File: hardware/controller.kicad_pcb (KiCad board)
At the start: 2 copper layers, 73.7 x 76.2 mm, 65 parts, among them J1 USB_B_Micro, J2 AVR-ISP-6, Q1 AO3402, Q10 AO3402, Q11 AO3402, Q12 AO3402, Q13 AO3402, Q14 AO3402, Q15 AO3402, Q16 AO3402, Q2 AO3402, Q3 AO3402, Q4 AO3402, Q5 AO3402, Q6 AO3402, Q7 AO3402, Q8 AO3402, Q9 AO3402, SW1 SW_Push_NO_NC_LED, SW10 SW_Push_NO_NC_LED, SW11 SW_Push_NO_NC_LED, SW12 SW_Push_NO_NC_LED, SW13 SW_Push_NO_NC_LED, SW14 SW_Push_NO_NC_LED, SW15 SW_Push_NO_NC_LED, SW16 SW_Push_NO_NC_LED, SW2 SW_Push_NO_NC_LED, SW3 SW_Push_NO_NC_LED, SW4 SW_Push_NO_NC_LED, SW5 SW_Push_NO_NC_LED, SW6 SW_Push_NO_NC_LED, SW7 SW_Push_NO_NC_LED, SW8 SW_Push_NO_NC_LED, SW9 SW_Push_NO_NC_LED, U1 CH340C, U2 ATmega328-AU, U3 MCP23017_SS, U4 PCA9685PW, Y1 14.7456 Mhz

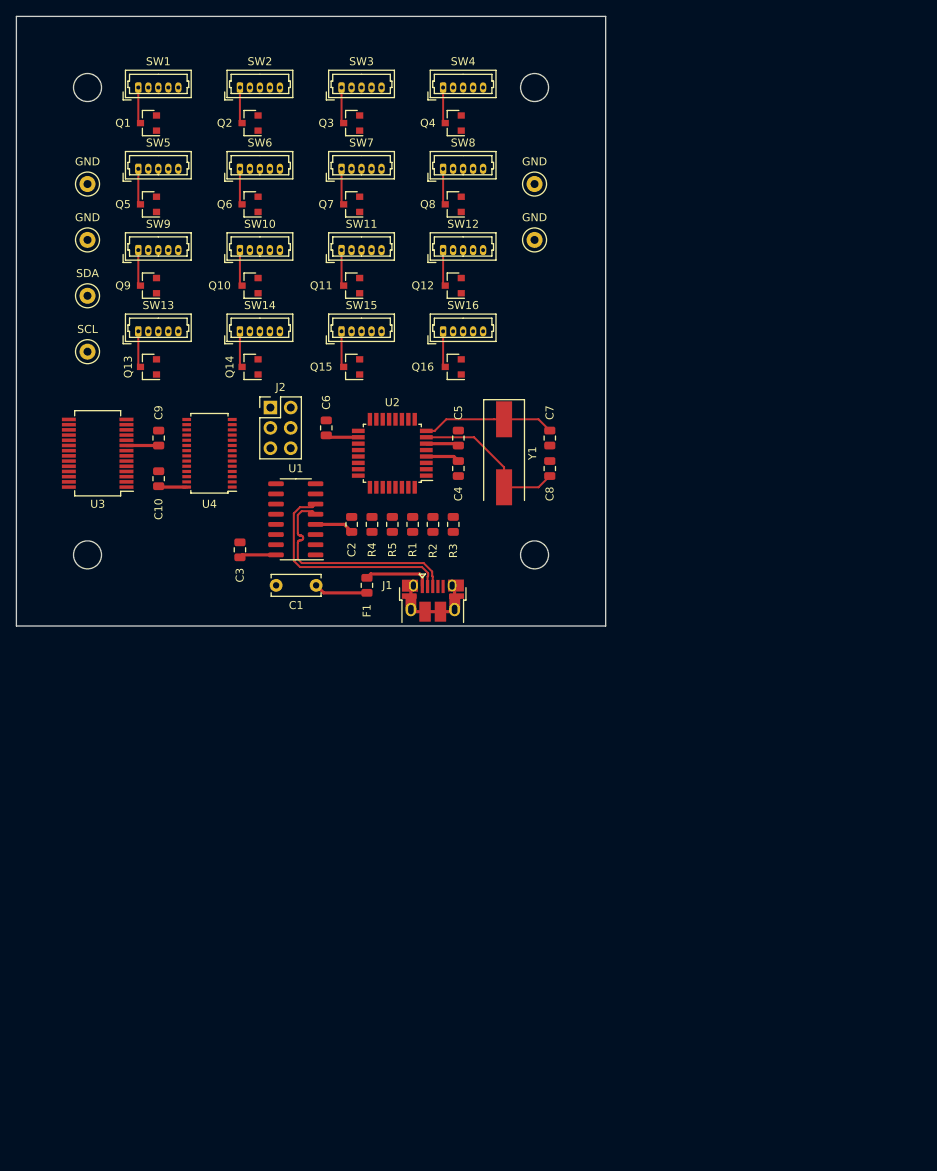
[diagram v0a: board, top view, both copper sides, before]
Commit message: create routing-friendly PCB layout and route it manually
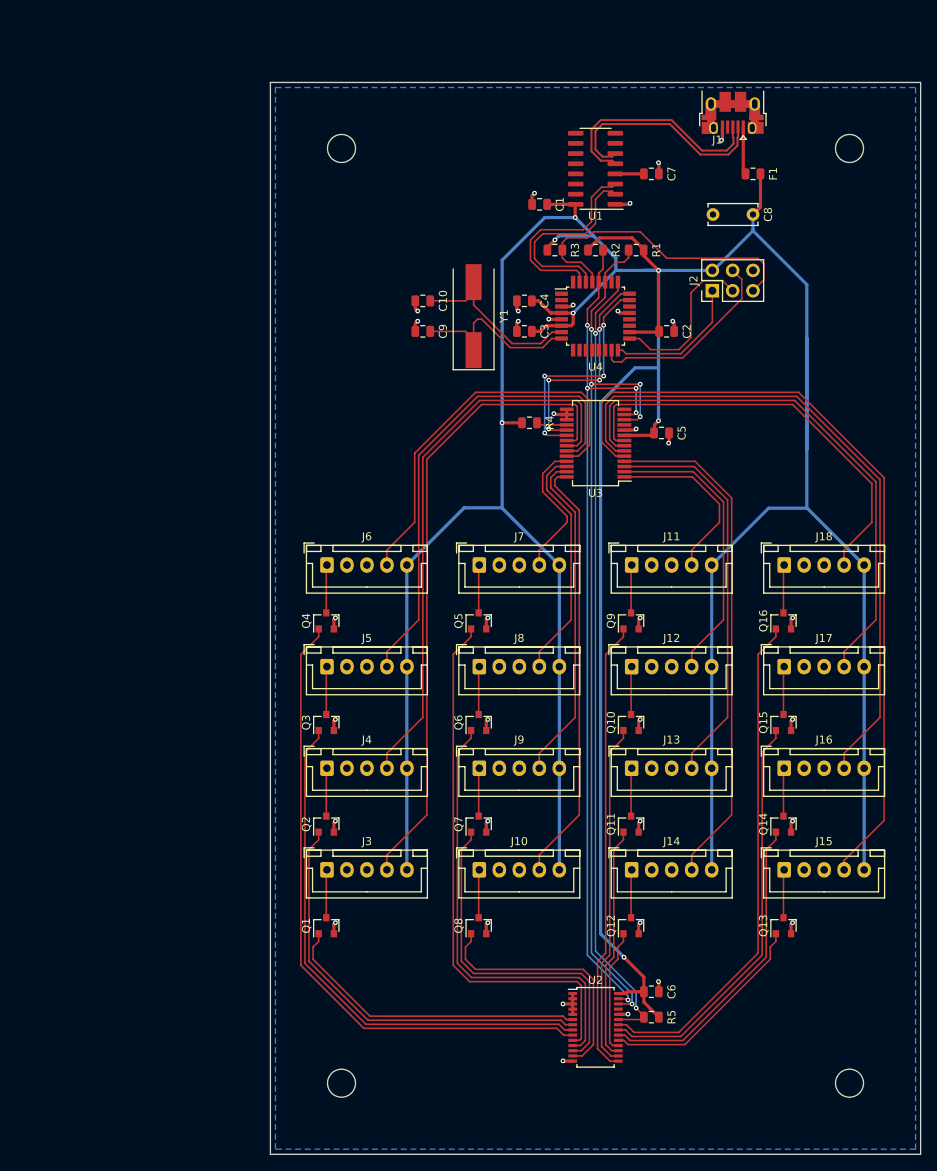
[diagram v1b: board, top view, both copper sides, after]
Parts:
- removed SW1, SW10, SW11, SW12, SW13, SW14, SW15, SW16, SW2, SW3, SW4, SW5, SW6, SW7, SW8, SW9: SW_Push_NO_NC_LED, Connector_Molex:Molex_PicoBlade_53047-0510_1x05_P1.25mm_Vertical
- removed TP1: SDA, TestPoint:TestPoint_Loop_D1.80mm_Drill1.0mm_Beaded
- removed TP2: SCL, TestPoint:TestPoint_Loop_D1.80mm_Drill1.0mm_Beaded
- removed TP3, TP4, TP5, TP6: GND, TestPoint:TestPoint_Loop_D1.80mm_Drill1.0mm_Beaded
- added J10: Conn_01x05_Male, Connector_JST:JST_XH_B5B-XH-A_1x05_P2.50mm_Vertical, F.Cu at (115.0, 147.3)
- added J11: Conn_01x05_Male, Connector_JST:JST_XH_B5B-XH-A_1x05_P2.50mm_Vertical, F.Cu at (134.1, 109.2)
- added J12: Conn_01x05_Male, Connector_JST:JST_XH_B5B-XH-A_1x05_P2.50mm_Vertical, F.Cu at (134.1, 121.9)
- added J13: Conn_01x05_Male, Connector_JST:JST_XH_B5B-XH-A_1x05_P2.50mm_Vertical, F.Cu at (134.1, 134.6)
- added J14: Conn_01x05_Male, Connector_JST:JST_XH_B5B-XH-A_1x05_P2.50mm_Vertical, F.Cu at (134.1, 147.3)
- added J15: Conn_01x05_Male, Connector_JST:JST_XH_B5B-XH-A_1x05_P2.50mm_Vertical, F.Cu at (153.1, 147.3)
- added J16: Conn_01x05_Male, Connector_JST:JST_XH_B5B-XH-A_1x05_P2.50mm_Vertical, F.Cu at (153.1, 134.6)
- added J17: Conn_01x05_Male, Connector_JST:JST_XH_B5B-XH-A_1x05_P2.50mm_Vertical, F.Cu at (153.1, 121.9)
- added J18: Conn_01x05_Male, Connector_JST:JST_XH_B5B-XH-A_1x05_P2.50mm_Vertical, F.Cu at (153.1, 109.2)
- added J3: Conn_01x05_Male, Connector_JST:JST_XH_B5B-XH-A_1x05_P2.50mm_Vertical, F.Cu at (96.0, 147.3)
- added J4: Conn_01x05_Male, Connector_JST:JST_XH_B5B-XH-A_1x05_P2.50mm_Vertical, F.Cu at (96.0, 134.6)
- added J5: Conn_01x05_Male, Connector_JST:JST_XH_B5B-XH-A_1x05_P2.50mm_Vertical, F.Cu at (96.0, 121.9)
- added J6: Conn_01x05_Male, Connector_JST:JST_XH_B5B-XH-A_1x05_P2.50mm_Vertical, F.Cu at (96.0, 109.2)
- added J7: Conn_01x05_Male, Connector_JST:JST_XH_B5B-XH-A_1x05_P2.50mm_Vertical, F.Cu at (115.0, 109.2)
- added J8: Conn_01x05_Male, Connector_JST:JST_XH_B5B-XH-A_1x05_P2.50mm_Vertical, F.Cu at (115.0, 121.9)
- added J9: Conn_01x05_Male, Connector_JST:JST_XH_B5B-XH-A_1x05_P2.50mm_Vertical, F.Cu at (115.0, 134.6)
- C1: value 10u -> 100n; footprint Capacitor_THT:C_Disc_D6.0mm_W2.5mm_P5.00mm -> Capacitor_SMD:C_0805_2012Metric
- C10, C9: value 100n -> 22p
- C7: value 22p -> 100n
- C8: value 22p -> 10u; footprint Capacitor_SMD:C_0805_2012Metric -> Capacitor_THT:C_Disc_D6.0mm_W2.5mm_P5.00mm
- U2: value ATmega328-AU -> PCA9685PW; footprint Package_QFP:TQFP-32_7x7mm_P0.8mm -> Package_SO:TSSOP-28_4.4x9.7mm_P0.65mm
- U4: value PCA9685PW -> ATmega328-AU; footprint Package_SO:TSSOP-28_4.4x9.7mm_P0.65mm -> Package_QFP:TQFP-32_7x7mm_P0.8mm
- moved Q13 105.7 mm to (153.0, 154.3), turned to 90 degrees
- moved Q1 102.8 mm to (95.9, 154.3), turned to 90 degrees
- moved Q8 90.2 mm to (114.9, 154.3), turned to 90 degrees
- moved Q2 88.1 mm to (95.9, 141.6), turned to 90 degrees
- moved Q14 87.8 mm to (153.0, 141.6), turned to 90 degrees
- moved Q12 83.0 mm to (134.0, 154.3), turned to 90 degrees
- moved C6 81.4 mm to (136.5, 162.6), turned to 0 degrees
- moved Q7 79.1 mm to (114.9, 141.6), turned to 90 degrees
- moved H4 76.9 mm to (161.3, 174.0)
- moved U2 76.1 mm to (129.5, 167.0), turned to 0 degrees
- moved Q11 75.8 mm to (134.0, 141.6), turned to 90 degrees
- moved Q3 75.0 mm to (95.9, 128.9), turned to 90 degrees
- moved Q9 73.5 mm to (134.0, 116.2), turned to 90 degrees
- moved H3 73.3 mm to (97.8, 174.0)
- moved Q10 72.5 mm to (134.0, 128.9), turned to 90 degrees
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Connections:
- C10 pad 1: +5V -> XTAL1
- C2 pad 1: GND -> +5V
- C2 pad 2: Net-(C2-Pad2) -> GND
- C7 pad 1: XTAL2 -> GND
- C7 pad 2: GND -> Net-(C7-Pad2)
- C8 pad 1: XTAL1 -> +5V
- C9 pad 1: +5V -> XTAL2
- Q10 pad 1: LEDx6 -> LEDx9
- Q12 pad 1: LEDxE -> LEDxB
- Q13 pad 1: LEDx3 -> LEDxC
- Q14 pad 1: LEDx7 -> LEDxD
- Q15 pad 1: LEDxB -> LEDxE
- Q2 pad 1: LEDx4 -> LEDx1
- Q3 pad 1: LEDx8 -> LEDx2
- Q4 pad 1: LEDxC -> LEDx3
- Q5 pad 1: LEDx1 -> LEDx4
- Q7 pad 1: LEDx9 -> LEDx6
- Q8 pad 1: LEDxD -> LEDx7
- Q9 pad 1: LEDx2 -> LEDx8
- R4 pad 1: GND -> +5V
- U1 pad 4: Net-(C2-Pad2) -> Net-(C7-Pad2)
- U2 pad 1: (no net) -> GND
- U2 pad 10: (no net) -> LEDx4
- U2 pad 11: (no net) -> LEDx5
- U2 pad 12: (no net) -> LEDx6
- U2 pad 13: (no net) -> LEDx7
- U2 pad 14: (no net) -> GND
- U2 pad 15: MOSI -> LEDx8
- U2 pad 16: MISO -> LEDx9
- U2 pad 17: SCK -> LEDxA
- U2 pad 18: +5V -> LEDxB
- U2 pad 19: (no net) -> LEDxC
- U2 pad 2: (no net) -> GND
- U2 pad 20: (no net) -> LEDxD
- U2 pad 21: GND -> LEDxE
- U2 pad 22: (no net) -> LEDxF
- U2 pad 23: INTA -> PCA9685.~OE
- U2 pad 24: INTB -> GND
- U2 pad 25: MCP23017.~RESET -> (no net)
- U2 pad 26: PCA9685.~OE -> SCL
- U2 pad 27: SCL -> SDA
- U2 pad 28: SDA -> +5V
- U2 pad 4: +5V -> GND
- U2 pad 6: +5V -> LEDx0
- U2 pad 7: XTAL1 -> LEDx1
- U2 pad 8: XTAL2 -> LEDx2
- U2 pad 9: (no net) -> LEDx3
- U4 pad 1: GND -> (no net)
- U4 pad 10: LEDx4 -> (no net)
- U4 pad 11: LEDx5 -> (no net)
- U4 pad 12: LEDx6 -> (no net)
- U4 pad 13: LEDx7 -> (no net)
- U4 pad 14: GND -> (no net)
- U4 pad 15: LEDx8 -> MOSI
- U4 pad 16: LEDx9 -> MISO
- U4 pad 17: LEDxA -> SCK
- U4 pad 18: LEDxB -> +5V
- U4 pad 19: LEDxC -> (no net)
- U4 pad 2: GND -> (no net)
- U4 pad 20: LEDxD -> (no net)
- U4 pad 21: LEDxE -> GND
- U4 pad 22: LEDxF -> (no net)
- U4 pad 23: PCA9685.~OE -> INTA
- U4 pad 24: GND -> INTB
- U4 pad 25: (no net) -> PCA9685.~OE
- U4 pad 26: SCL -> (no net)
- U4 pad 27: SDA -> SCL
- U4 pad 28: +5V -> SDA
- U4 pad 4: GND -> +5V
- U4 pad 6: LEDx0 -> +5V
- U4 pad 7: LEDx1 -> XTAL1
- U4 pad 8: LEDx2 -> XTAL2
- U4 pad 9: LEDx3 -> (no net)
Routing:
- net +5V: track 31.4 -> 507.8 mm, vias 0 -> 7
- net SCL: track 0.00 -> 112.9 mm, vias 0 -> 5
- net SDA: track 0.00 -> 108.6 mm, vias 0 -> 5
- net BTNxC: track 0.00 -> 99.9 mm
- net PCA9685.~OE: track 0.00 -> 98.9 mm, vias 0 -> 2
- net BTNxD: track 0.00 -> 84.3 mm
- net BTNx0: track 0.00 -> 80.6 mm
- net LEDx3: track 0.00 -> 80.6 mm
- net BTNx1: track 0.00 -> 70.3 mm
- net BTNxE: track 0.00 -> 68.9 mm
- net LEDx4: track 0.00 -> 67.8 mm
- net LEDx2: track 0.00 -> 66.7 mm
- net BTNxB: track 0.00 -> 63.9 mm
- net LEDxF: track 0.00 -> 63.4 mm
- net BTNx2: track 0.00 -> 60.1 mm
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- added copper zone on B.Cu, net GND
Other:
- board size 73.7 x 76.2 mm -> 81.3 x 134 mm
- net class Default: clearance 0.15 -> 0.1; trace_width 0.25 -> 0.2
- net class Shield added: clearance 0.2, trace_width 1, via_dia 0.6, via_drill 0.3
- rule trace_clearance: 0.15 -> 0.1

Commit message: change USB connector, finalize PCB shape
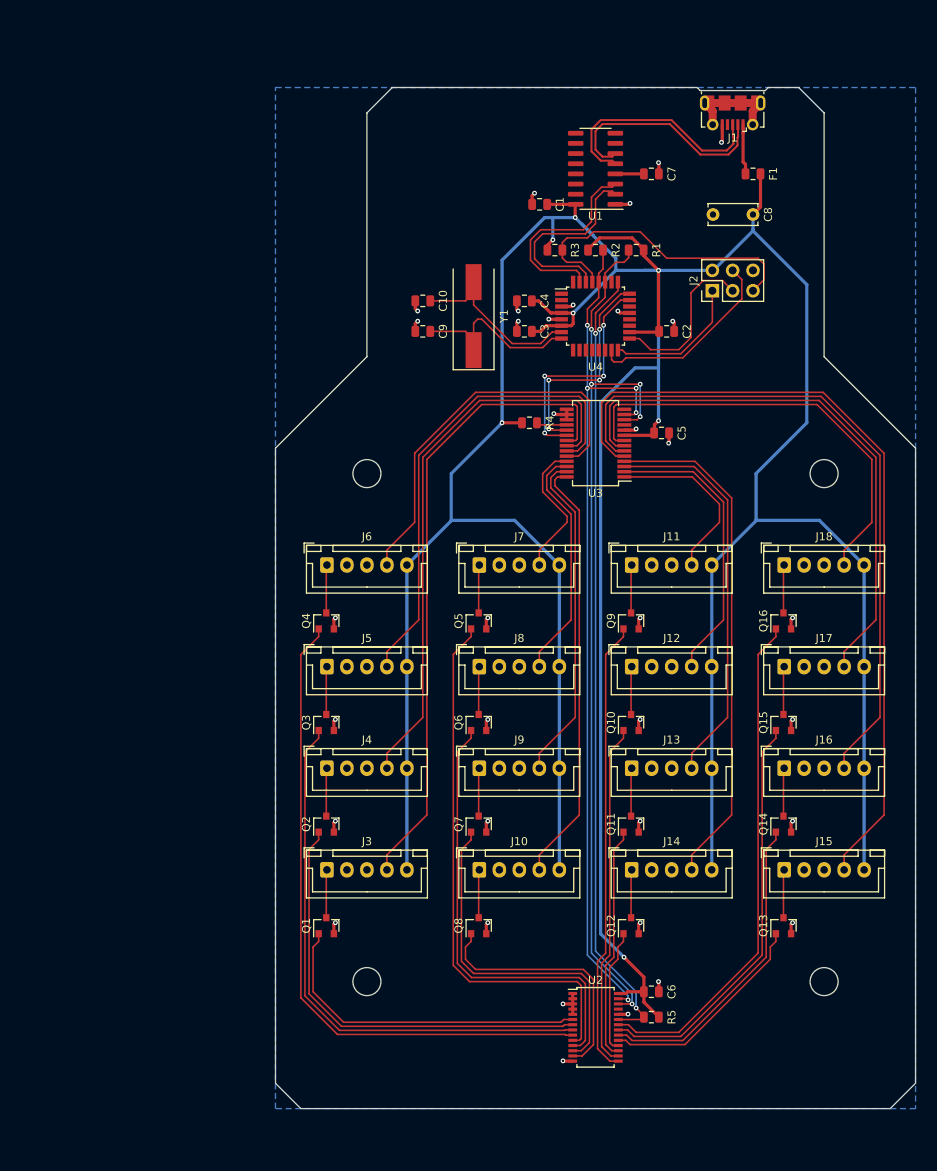
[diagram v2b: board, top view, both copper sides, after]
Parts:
- J1: footprint Connector_USB:USB_Micro-B_Amphenol_10103594-0001LF_Horizontal -> Connector_USB:USB_Micro-B_Molex-105017-0001
- moved H1 40.8 mm to (101.0, 97.8)
- moved H2 40.8 mm to (158.1, 97.8)
- moved H3 13.1 mm to (101.0, 161.3)
- moved H4 13.1 mm to (158.1, 161.3)
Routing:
- net +5V: track 507.8 -> 499.4 mm
- net LEDx0: track 39.1 -> 41.7 mm
- net LEDx1: track 52.9 -> 55.4 mm
- net LEDx2: track 66.7 -> 69.2 mm
- net LEDx3: track 80.6 -> 82.9 mm
- net BTNxD: track 84.3 -> 86.1 mm
- net BTNxF: track 53.4 -> 55.2 mm
- net BTNxC: track 99.9 -> 101.6 mm
- net BTNxE: track 68.9 -> 70.7 mm
- net Net-(J1-Pad6): track 11.7 -> 12.6 mm
- net GND: track 54.8 -> 55.3 mm
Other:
- board size 81.3 x 134 mm -> 80 x 127.6 mm

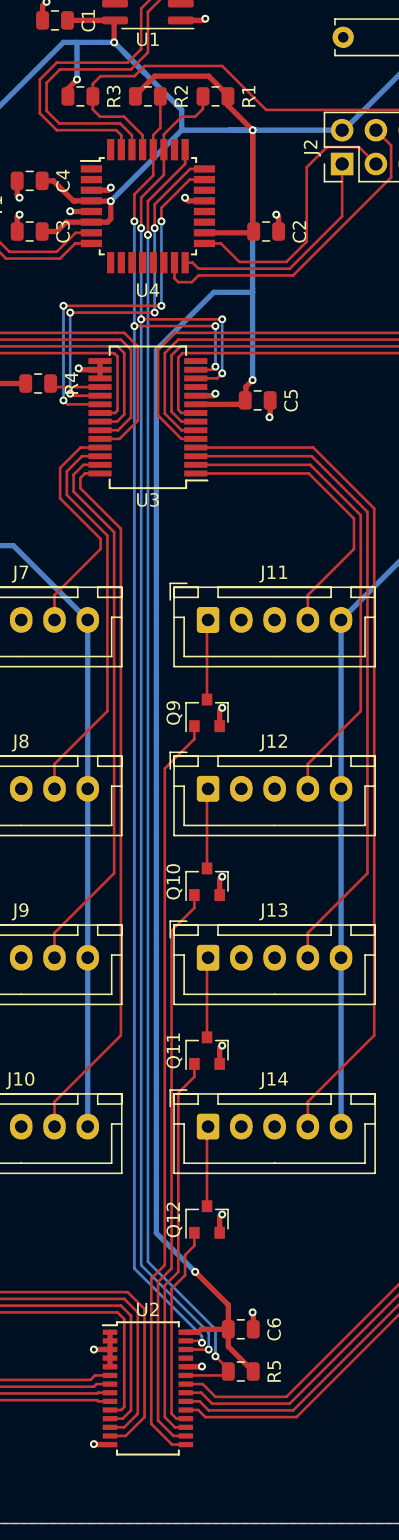
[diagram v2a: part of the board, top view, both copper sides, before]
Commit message: fix assignment of SCL and SDA pins on ATmega328p
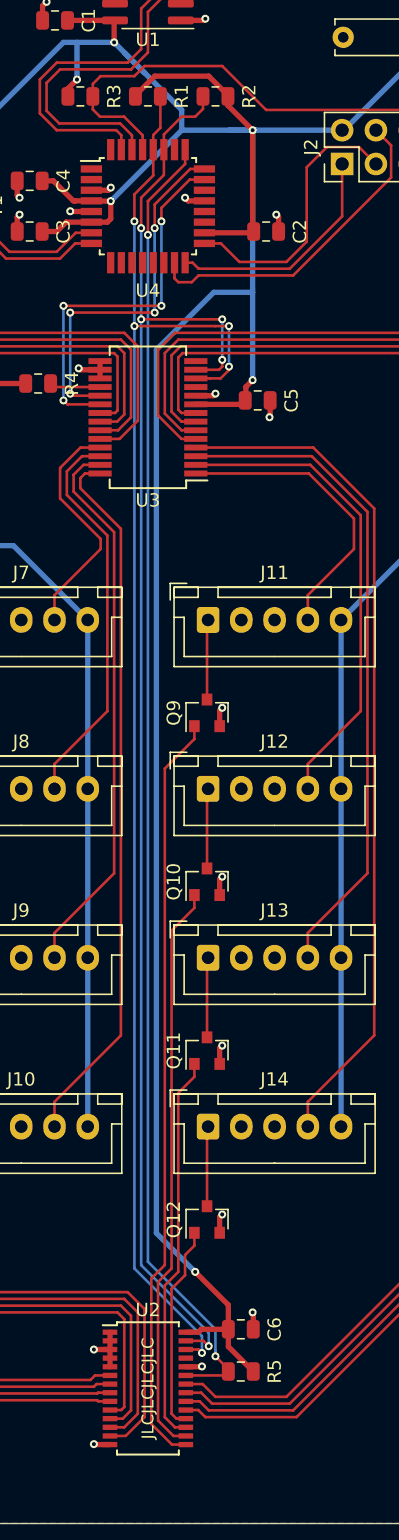
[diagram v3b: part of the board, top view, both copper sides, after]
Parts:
- U4: value ATmega328-AU -> ATmega328P-MU
- moved R1 5.08 mm to (129.5, 69.8), turned to 180 degrees
- moved R2 5.08 mm to (134.6, 69.8), turned to 0 degrees
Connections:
- U4 pad 27: SCL -> SDA
- U4 pad 28: SDA -> SCL
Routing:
- net SDA: track 108.6 -> 112.2 mm
- net SCL: track 112.9 -> 111.9 mm
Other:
- board text added: "JLCJLCJLCJLC"

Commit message: use 36pF capacitors for crystal
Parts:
- C10, C9: value 22p -> 36p
- U4: value ATmega328P-MU -> ATmega328P-AU
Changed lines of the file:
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@@
     (add_net MISO)
     (add_net MOSI)
+    (add_net "Net-(J1-Pad4)")
     (add_net "Net-(J10-Pad1)")
+    (add_net "Net-(J10-Pad2)")
     (add_net "Net-(J11-Pad1)")
+    (add_net "Net-(J11-Pad2)")
     (add_net "Net-(J12-Pad1)")
+    (add_net "Net-(J12-Pad2)")
     (add_net "Net-(J13-Pad1)")
+    (add_net "Net-(J13-Pad2)")
     (add_net "Net-(J14-Pad1)")
+    (add_net "Net-(J14-Pad2)")
     (add_net "Net-(J15-Pad1)")
+    (add_net "Net-(J15-Pad2)")
     (add_net "Net-(J16-Pad1)")
+    (add_net "Net-(J16-Pad2)")
     (add_net "Net-(J17-Pad1)")
+    (add_net "Net-(J17-Pad2)")
     (add_net "Net-(J18-Pad1)")
+    (add_net "Net-(J18-Pad2)")
     (add_net "Net-(J3-Pad1)")
+    (add_net "Net-(J3-Pad2)")
     (add_net "Net-(J4-Pad1)")
+    (add_net "Net-(J4-Pad2)")
     (add_net "Net-(J5-Pad1)")
+    (add_net "Net-(J5-Pad2)")
     (add_net "Net-(J6-Pad1)")
+    (add_net "Net-(J6-Pad2)")
     (add_net "Net-(J7-Pad1)")
+    (add_net "Net-(J7-Pad2)")
     (add_net "Net-(J8-Pad1)")
+    (add_net "Net-(J8-Pad2)")
     (add_net "Net-(J9-Pad1)")
+    (add_net "Net-(J9-Pad2)")
+    (add_net "Net-(U1-Pad10)")
+    (add_net "Net-(U1-Pad11)")
+    (add_net "Net-(U1-Pad12)")
+    (add_net "Net-(U1-Pad13)")
+    (add_net "Net-(U1-Pad14)")
+    (add_net "Net-(U1-Pad15)")
+    (add_net "Net-(U1-Pad7)")
+    (add_net "Net-(U1-Pad8)")
+    (add_net "Net-(U1-Pad9)")
+    (add_net "Net-(U2-Pad25)")
+    (add_net "Net-(U3-Pad11)")
+    (add_net "Net-(U3-Pad14)")
+    (add_net "Net-(U4-Pad1)")
+    (add_net "Net-(U4-Pad10)")
+    (add_net "Net-(U4-Pad11)")
+    (add_net "Net-(U4-Pad12)")
+    (add_net "Net-(U4-Pad13)")
+    (add_net "Net-(U4-Pad14)")
+    (add_net "Net-(U4-Pad19)")
+    (add_net "Net-(U4-Pad2)")
+    (add_net "Net-(U4-Pad20)")
+    (add_net "Net-(U4-Pad22)")
+    (add_net "Net-(U4-Pad26)")
+    (add_net "Net-(U4-Pad32)")
+    (add_net "Net-(U4-Pad9)")
     (add_net PCA9685.~OE)
     (add_net RXD)
@@
       (effects (font (size 1 1) (thickness 0.15)))
     )
-    (fp_text value ATmega328P-MU (at 0 6.05) (layer F.Fab)
+    (fp_text value ATmega328P-AU (at 0 6.05) (layer F.Fab)
       (effects (font (size 1 1) (thickness 0.15)))
     )
@@
       (effects (font (size 1 1) (thickness 0.15)))
     )
-    (fp_text value 22p (at 0 1.65) (layer F.Fab)
+    (fp_text value 36p (at 0 1.65) (layer F.Fab)
       (effects (font (size 1 1) (thickness 0.15)))
     )
@@
       (effects (font (size 1 1) (thickness 0.15)))
     )
-    (fp_text value 22p (at 0 1.65) (layer F.Fab)
+    (fp_text value 36p (at 0 1.65) (layer F.Fab)
       (effects (font (size 1 1) (thickness 0.15)))
     )
@@
   (segment (start 129.536 54.967554) (end 129.536 57.300446) (width 0.25) (layer F.Cu) (net 11))
   (segment (start 147.285 55.782501) (end 147.285 56.776554) (width 0.25) (layer F.Cu) (net 11))
-  (segment (start 133.6825 70.7875) (end 133.6825 69.85) (width 0.2) (layer F.Cu) (net 13))
-  (segment (start 133.096 71.374) (end 133.6825 70.7875) (width 0.2) (layer F.Cu) (net 13))
-  (segment (start 132.08 71.374) (end 133.096 71.374) (width 0.2) (layer F.Cu) (net 13))
-  (segment (start 130.74 72.714) (end 132.08 71.374) (width 0.2) (layer F.Cu) (net 13))
-  (segment (start 130.74 73.855) (end 130.74 72.714) (width 0.2) (layer F.Cu) (net 13))
-  (via (at 129.032 79.756) (size 0.6) (drill 0.3) (layers F.Cu B.Cu) (net 13))
-  (segment (start 130.74 75.762) (end 130.74 73.855) (width 0.2) (layer F.Cu) (net 13))
-  (segment (start 129.032 77.47) (end 130.74 75.762) (width 0.2) (layer F.Cu) (net 13))
-  (segment (start 129.032 79.756) (end 129.032 77.47) (width 0.2) (layer F.Cu) (net 13))
-  (segment (start 129.032 79.756) (end 129.032 86.614) (width 0.2) (layer B.Cu) (net 13))
-  (segment (start 129.032 157.734) (end 134.112 162.814) (width 0.2) (layer B.Cu) (net 13))
-  (segment (start 129.032 86.614) (end 129.032 157.734) (width 0.2) (layer B.Cu) (net 13))
   (segment (start 130.4775 72.2145) (end 130.4775 69.85) (width 0.2) (layer F.Cu) (net 12))
   (segment (start 129.94 72.752) (end 130.4775 72.2145) (width 0.2) (layer F.Cu) (net 12))
@@
   (segment (start 135.636 90.424) (end 135.005 91.055) (width 0.2) (layer F.Cu) (net 12))
   (segment (start 135.636 90.17) (end 135.636 90.424) (width 0.2) (layer F.Cu) (net 12))
+  (segment (start 133.6825 70.7875) (end 133.6825 69.85) (width 0.2) (layer F.Cu) (net 13))
+  (segment (start 133.096 71.374) (end 133.6825 70.7875) (width 0.2) (layer F.Cu) (net 13))
+  (segment (start 132.08 71.374) (end 133.096 71.374) (width 0.2) (layer F.Cu) (net 13))
+  (segment (start 130.74 72.714) (end 132.08 71.374) (width 0.2) (layer F.Cu) (net 13))
+  (segment (start 130.74 73.855) (end 130.74 72.714) (width 0.2) (layer F.Cu) (net 13))
+  (via (at 129.032 79.756) (size 0.6) (drill 0.3) (layers F.Cu B.Cu) (net 13))
+  (segment (start 130.74 75.762) (end 130.74 73.855) (width 0.2) (layer F.Cu) (net 13))
+  (segment (start 129.032 77.47) (end 130.74 75.762) (width 0.2) (layer F.Cu) (net 13))
+  (segment (start 129.032 79.756) (end 129.032 77.47) (width 0.2) (layer F.Cu) (net 13))
+  (segment (start 129.032 79.756) (end 129.032 86.614) (width 0.2) (layer B.Cu) (net 13))
+  (segment (start 129.032 157.734) (end 134.112 162.814) (width 0.2) (layer B.Cu) (net 13))
+  (segment (start 129.032 86.614) (end 129.032 157.734) (width 0.2) (layer B.Cu) (net 13))
   (via (at 134.112 163.83) (size 0.6) (drill 0.3) (layers F.Cu B.Cu) (net 13))
   (segment (start 134.112 162.814) (end 134.112 163.83) (width 0.2) (layer B.Cu) (net 13))
